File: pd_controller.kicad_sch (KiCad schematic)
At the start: 33 parts, among them Q1 NVTR4503NT1G, Q2 IRF9358TRPBF, Q5 BSL308PEH6327XTSA1, SW1 SW_SPDT, U1 CYPD3177-24LQXQT

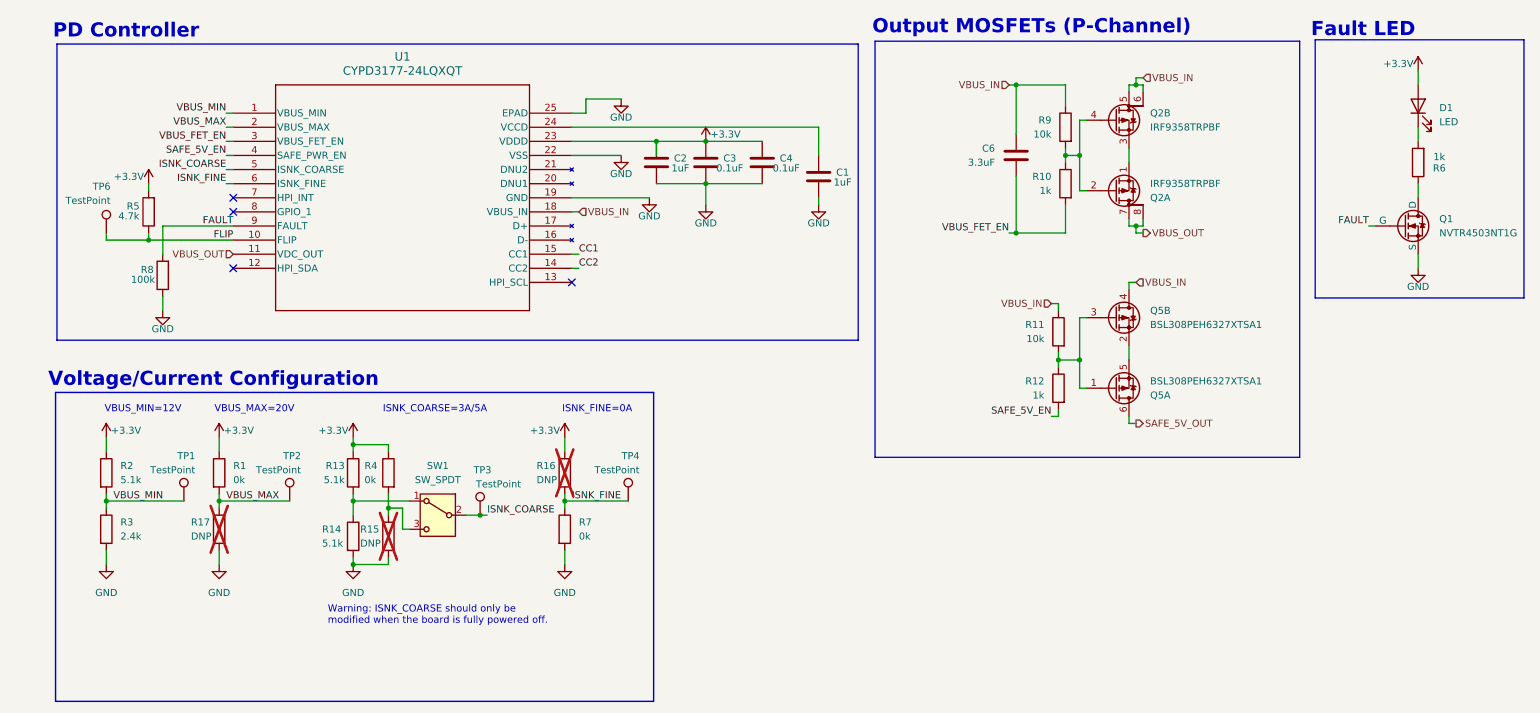
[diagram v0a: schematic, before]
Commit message: Finished 5V buck converter schematic
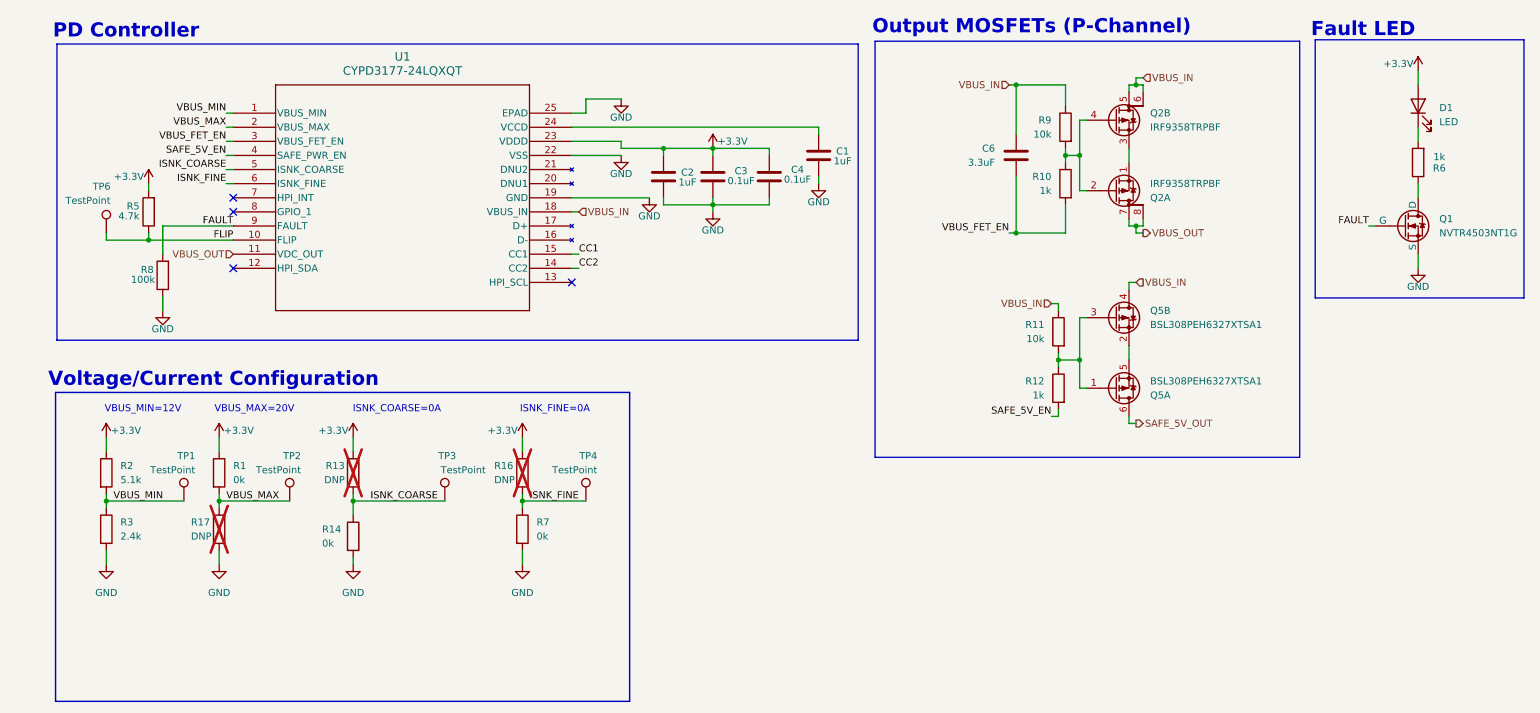
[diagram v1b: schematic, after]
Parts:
- removed R15: DNP, symbol Device:R
- removed R4: 0k, symbol Device:R
- removed SW1: SW_SPDT, symbol Switch:SW_SPDT
- R13: value 5.1k -> DNP; now not fitted
- R14: value 5.1k -> 0k
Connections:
- net ISNK_COARSE: now also R13.2, R14.1
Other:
- note added: "ISNK_COARSE=0A"
- note removed: "ISNK_COARSE=3A/5A"
- note removed: "Warning: ISNK_COARSE should only be modified when the board is fully powered off."
- company: (none) -> Longhorn Racing Solar
- moved on the sheet: C1, C2, C3, C4, R16, R7, TP3, TP4

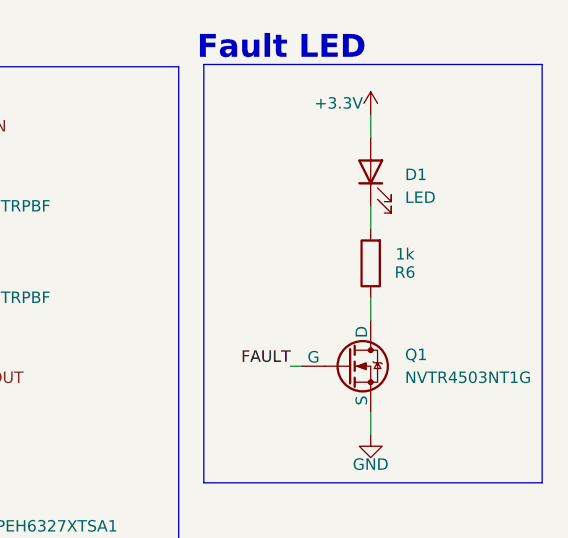
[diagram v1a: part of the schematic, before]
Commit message: added power good LED indicators
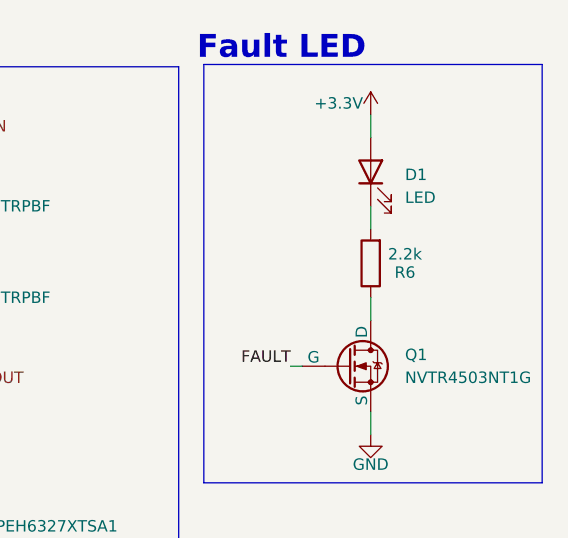
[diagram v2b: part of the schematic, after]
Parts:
- R6: value 1k -> 2.2k
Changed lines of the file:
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@@
 			)
 		)
-		(property "Value" "1k"
+		(property "Value" "2.2k"
 			(at 267.97 63.754 0)
 			(effects

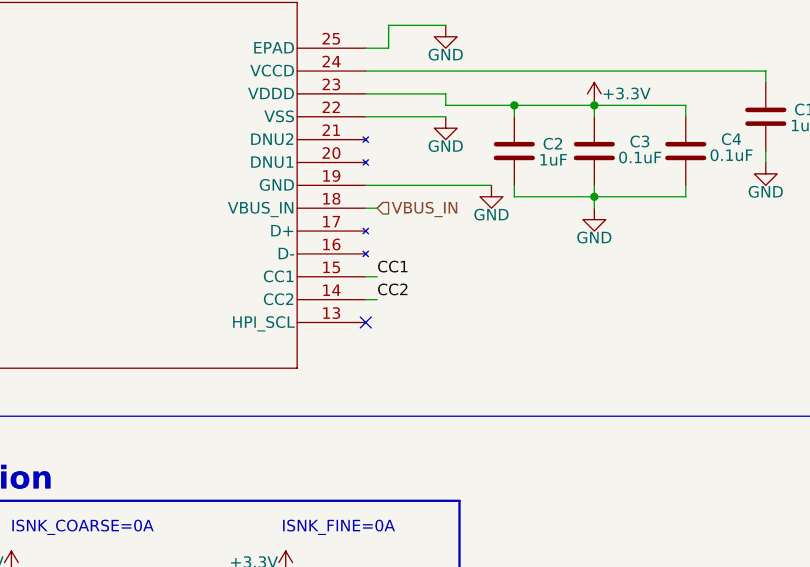
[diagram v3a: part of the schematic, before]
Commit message: changed to 1-channel chip for current sense & fixed ERC
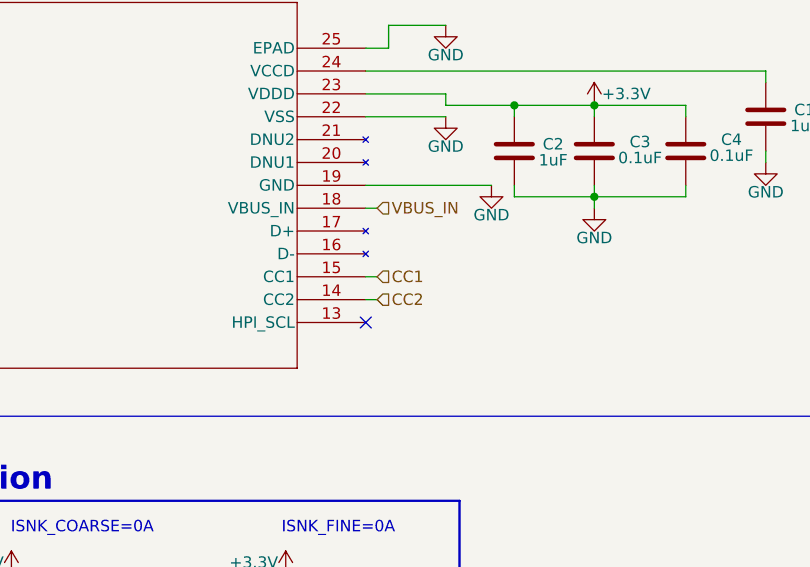
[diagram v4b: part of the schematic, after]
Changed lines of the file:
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@@
-		)
-	)
-	(label "CC1"
-		(at 113.03 81.28 0)
-		(fields_autoplaced yes)
-		(effects
-			(font
-				(size 1.27 1.27)
-			)
-			(justify left bottom)
 		)
 	)
@@
 			)
 			(justify right bottom)
-		)
-	)
-	(label "CC2"
-		(at 113.03 83.82 0)
-		(fields_autoplaced yes)
-		(effects
-			(font
-				(size 1.27 1.27)
-			)
-			(justify left bottom)
 		)
 	)
@@
 		(fields_autoplaced yes)
 		(effects
+			(font
+				(size 1.27 1.27)
+			)
+			(justify left)
+		)
+	)
+	(hierarchical_label "CC1"
+		(shape input)
+		(at 113.03 81.28 0)
+		(fields_autoplaced yes)
+		(effects
+			(font
+				(size 1.27 1.27)
+			)
+			(justify left)
+		)
+	)
+	(hierarchical_label "CC2"
+		(shape input)
+		(at 113.03 83.82 0)
+		(fields_autoplaced yes)
+		(effects

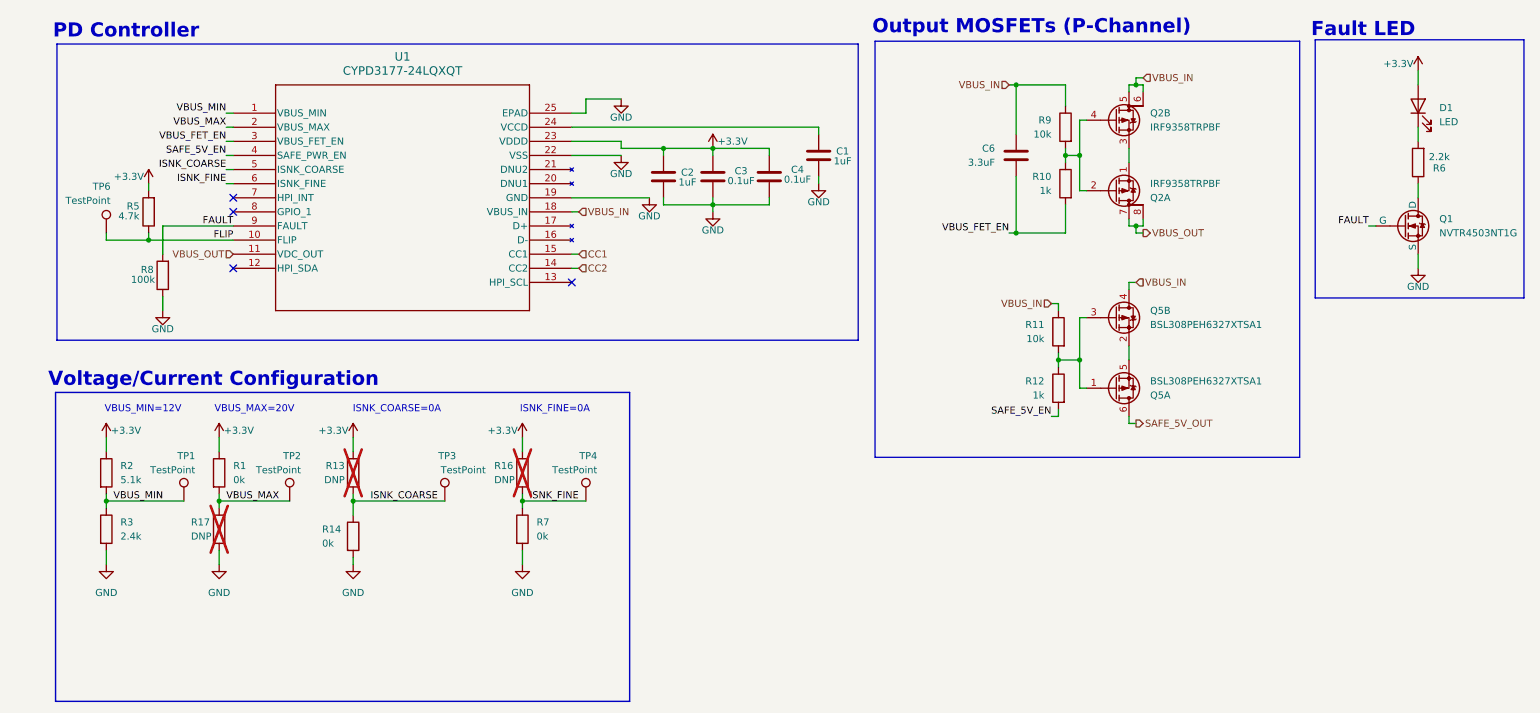
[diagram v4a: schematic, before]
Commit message: updated with some new footprints (have yet to finish footprint assignment; also need to switch out inductor for 5V buck)
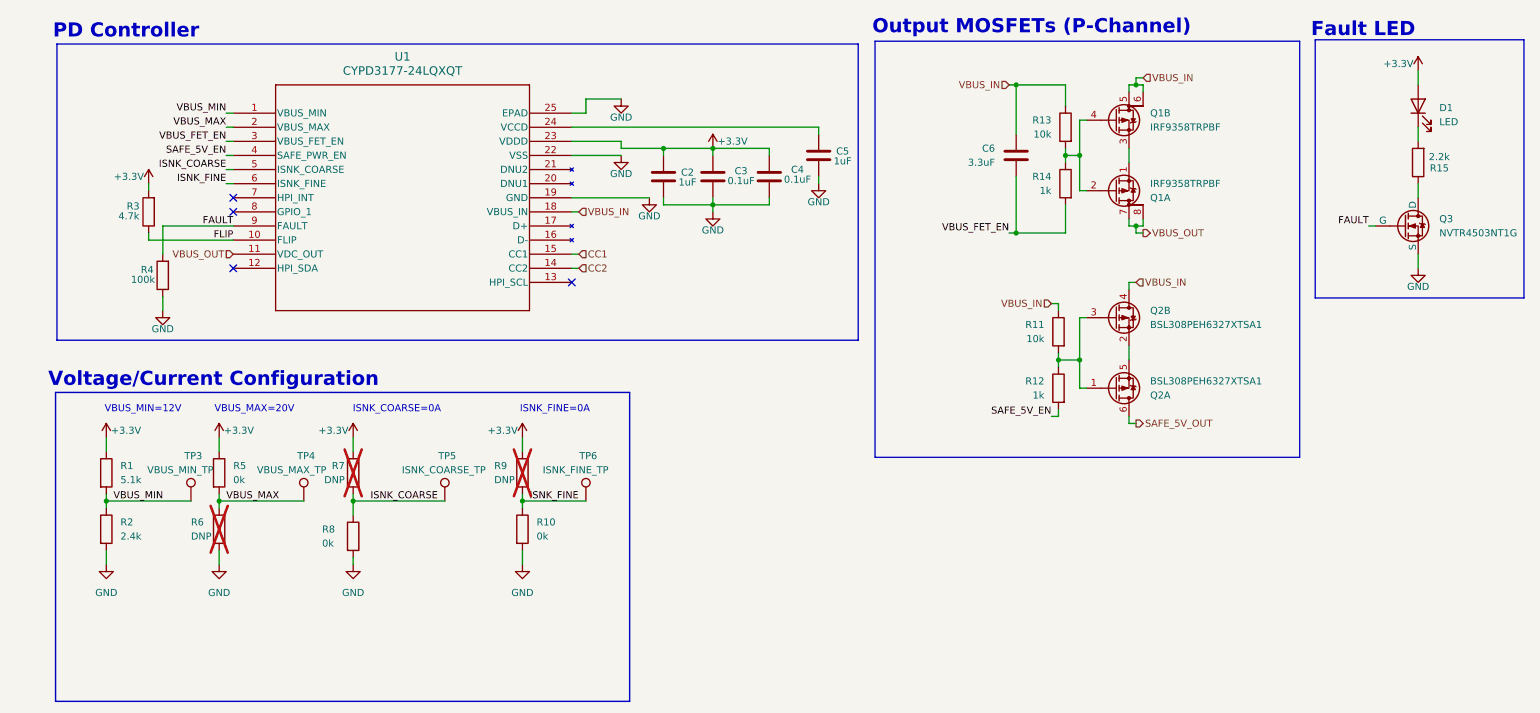
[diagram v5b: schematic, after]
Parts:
- removed TP6: TestPoint, symbol Connector:TestPoint
- C2, C3, C4, C6: footprint (none) -> Capacitor_SMD:C_0805_2012Metric
- C5: renamed from C1; footprint (none) -> Capacitor_SMD:C_0805_2012Metric
- R1: renamed from R2; footprint (none) -> Resistor_SMD:R_0805_2012Metric
- R10: renamed from R7; footprint (none) -> Resistor_SMD:R_0805_2012Metric
- R11, R12: footprint (none) -> Resistor_SMD:R_0805_2012Metric
- R13: renamed from R9; footprint (none) -> Resistor_SMD:R_0805_2012Metric
- R14: renamed from R10; footprint (none) -> Resistor_SMD:R_0805_2012Metric
- R15: renamed from R6; footprint (none) -> Resistor_SMD:R_0805_2012Metric
- R2: renamed from R3; footprint (none) -> Resistor_SMD:R_0805_2012Metric
- R3: renamed from R5; footprint (none) -> Resistor_SMD:R_0805_2012Metric
- R4: renamed from R8; footprint (none) -> Resistor_SMD:R_0805_2012Metric
- R5: renamed from R1; footprint (none) -> Resistor_SMD:R_0805_2012Metric
- R6: renamed from R17; footprint (none) -> Resistor_SMD:R_0805_2012Metric
- R7: renamed from R13; footprint (none) -> Resistor_SMD:R_0805_2012Metric
- R8: renamed from R14; footprint (none) -> Resistor_SMD:R_0805_2012Metric
- R9: renamed from R16; footprint (none) -> Resistor_SMD:R_0805_2012Metric
- TP3: renamed from TP1; value TestPoint -> VBUS_MIN_TP; footprint (none) -> TestPoint:TestPoint_Pad_D2.5mm
- TP4: renamed from TP2; value TestPoint -> VBUS_MAX_TP; footprint (none) -> TestPoint:TestPoint_Pad_D2.5mm
- TP5: renamed from TP3; value TestPoint -> ISNK_COARSE_TP; footprint (none) -> TestPoint:TestPoint_Pad_D2.5mm
- TP6: renamed from TP4; value TestPoint -> ISNK_FINE_TP; footprint (none) -> TestPoint:TestPoint_Pad_D2.5mm
- U1: footprint CYPD3177-24LQXQT_CYP -> UTSVT_ICs:CYPD3177-24LQXQT_CYP
- renumbered Q2 to Q1, Q5 to Q2, Q1 to Q3
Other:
- moved on the sheet: TP3, TP4

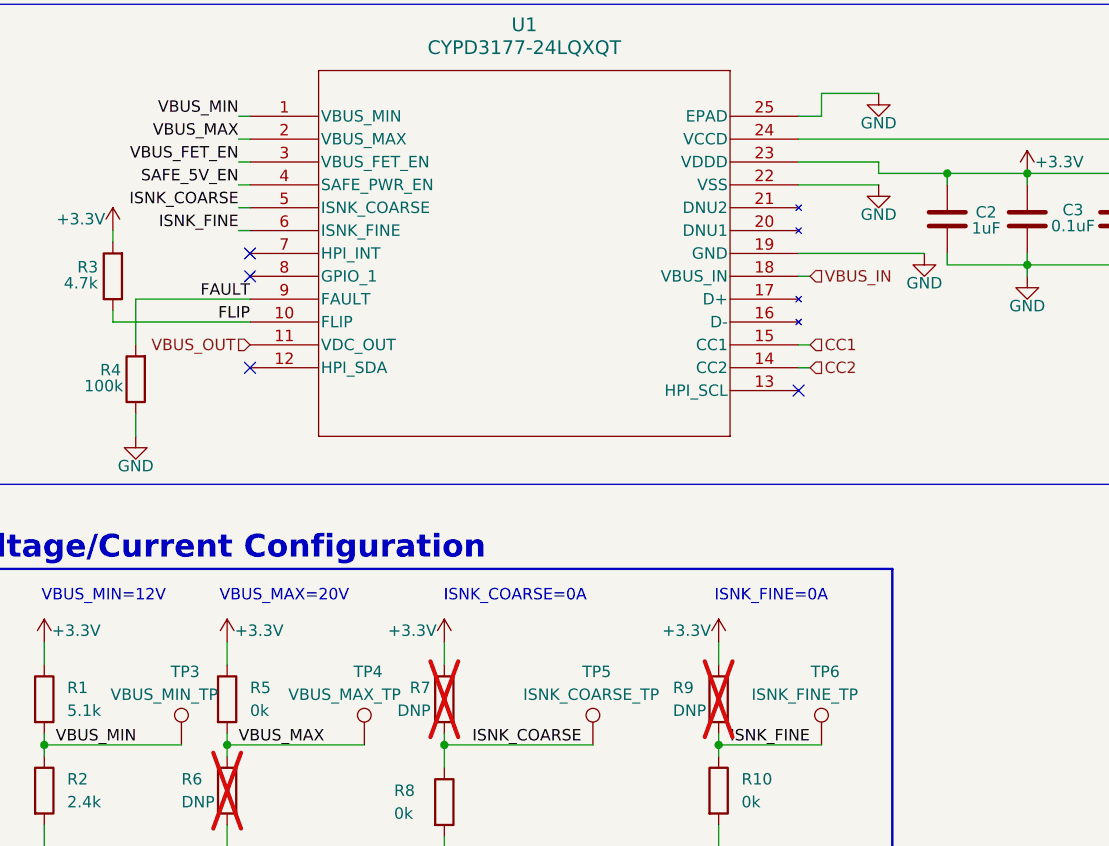
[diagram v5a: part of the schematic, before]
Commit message: almost done w/ schematic, just need to finish footprint assignment (make sure buck converter components are correctly chosen and there aren't caps that need to be different and stuff)
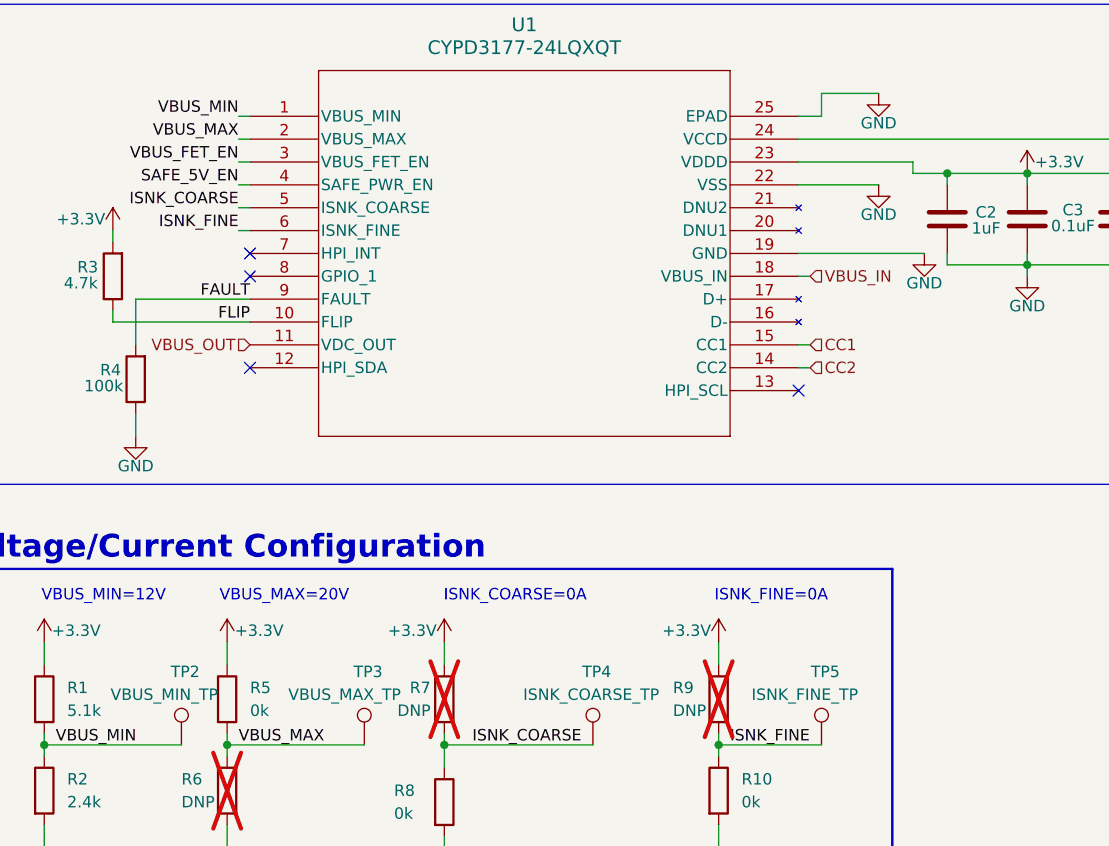
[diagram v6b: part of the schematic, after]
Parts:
- D1: footprint (none) -> LED_SMD:LED_0805_2012Metric; Mouser Part Number (none) -> APTD2012LCGCK
- renumbered TP3 to TP2, TP4 to TP3, TP5 to TP4, TP6 to TP5
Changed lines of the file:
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@@
 	(wire
 		(pts
-			(xy 27.94 114.3) (xy 27.94 116.84)
-		)
-		(stroke
-			(width 0)
-			(type default)
-		)
-	)
-	(wire
-		(pts
 			(xy 72.39 137.16) (xy 72.39 135.89)
 		)
@@
 	(wire
 		(pts
-			(xy 120.65 62.23) (xy 128.27 62.23)
+			(xy 124.46 62.23) (xy 128.27 62.23)
 		)
 		(stroke
@@
 	(wire
 		(pts
+			(xy 27.94 114.3) (xy 27.94 116.84)
+		)
+		(stroke
+			(width 0)
+			(type default)
+		)
+	)
+	(wire
+		(pts
 			(xy 120.65 53.34) (xy 114.3 53.34)
 		)
@@
 	(wire
 		(pts
-			(xy 120.65 62.23) (xy 120.65 60.96)
+			(xy 124.46 62.23) (xy 124.46 60.96)
 		)
 		(stroke
@@
 	(wire
 		(pts
-			(xy 120.65 60.96) (xy 111.76 60.96)
+			(xy 124.46 60.96) (xy 111.76 60.96)
 		)
 		(stroke
@@
 			)
 		)
-		(property "Footprint" ""
+		(property "Footprint" "LED_SMD:LED_0805_2012Metric"
 			(at 264.16 54.61 0)
 			(effects
@@
 			)
 		)
-		(property "Datasheet" "~"
+		(property "Datasheet" "https://www.mouser.com/datasheet/2/216/APTD2012LCGCK-1102037.pdf"
 			(at 264.16 54.61 0)
 			(effects
@@
 			)
 		)
+		(property "Mouser Part Number" "APTD2012LCGCK"
+			(at 264.16 54.61 0)
+			(effects
+				(font
+					(size 1.27 1.27)
+				)
+				(hide yes)
+			)
+		)
 		(pin "2"
 		)
@@
 		(on_board yes)
 		(dnp no)
-		(property "Reference" "TP5"
+		(property "Reference" "TP4"
 			(at 90.932 117.602 0)
 			(effects
@@
 			(project "USBCPowerPCB"
 				(path "/f58400c5-df4b-4929-8d2b-33c0fe23fcd9/4ed27f5f-caef-4817-8da2-6ac4f08dfb73"
-					(reference "TP5")
+					(reference "TP4")
 					(unit 1)
 				)
@@
 		(on_board yes)
 		(dnp no)
-		(property "Reference" "TP4"
+		(property "Reference" "TP3"
 			(at 65.532 117.602 0)
 			(effects
@@
 			(project "USBCPowerPCB"
 				(path "/f58400c5-df4b-4929-8d2b-33c0fe23fcd9/4ed27f5f-caef-4817-8da2-6ac4f08dfb73"
-					(reference "TP4")
+					(reference "TP3")
 					(unit 1)
 				)
@@
 		(on_board yes)
 		(dnp no)
-		(property "Reference" "TP6"
+		(property "Reference" "TP5"
 			(at 116.332 117.602 0)
 			(effects
@@
 			(project "USBCPowerPCB"
 				(path "/f58400c5-df4b-4929-8d2b-33c0fe23fcd9/4ed27f5f-caef-4817-8da2-6ac4f08dfb73"
-					(reference "TP6")
+					(reference "TP5")
 					(unit 1)
 				)
@@
 		(on_board yes)
 		(dnp no)
-		(property "Reference" "TP3"
+		(property "Reference" "TP2"
 			(at 45.212 117.602 0)
 			(effects
@@
 			(project "USBCPowerPCB"
 				(path "/f58400c5-df4b-4929-8d2b-33c0fe23fcd9/4ed27f5f-caef-4817-8da2-6ac4f08dfb73"
-					(reference "TP3")
+					(reference "TP2")
 					(unit 1)
 				)
